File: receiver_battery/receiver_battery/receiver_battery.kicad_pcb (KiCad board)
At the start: 2 copper layers, 88 x 157 mm, 36 parts, among them U1 NRF24L01_Breakout

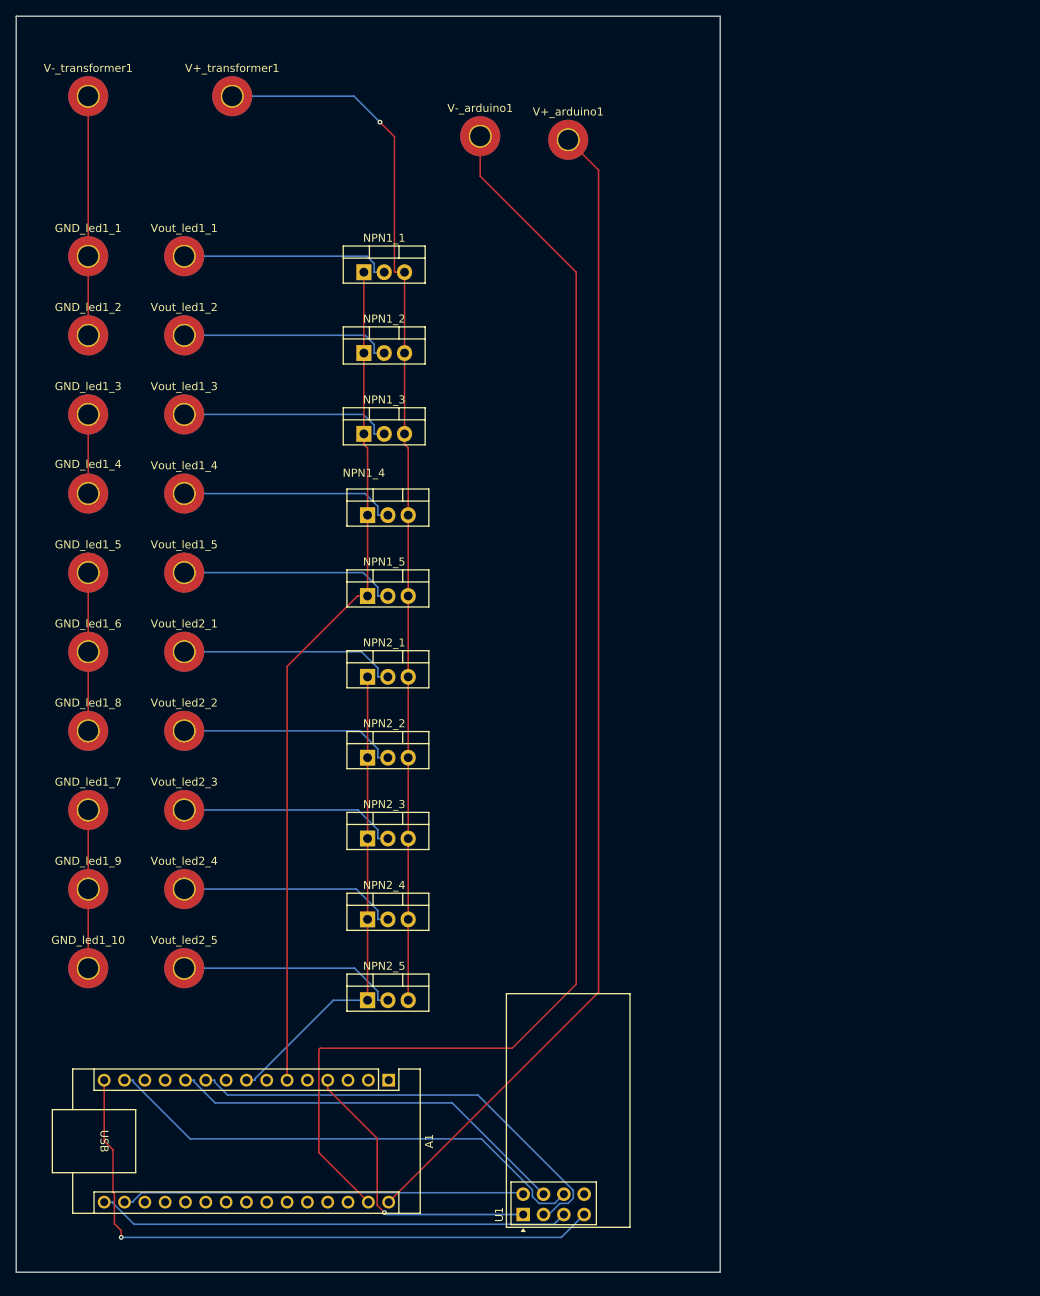
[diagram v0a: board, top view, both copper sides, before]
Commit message: pulldown on each transistor
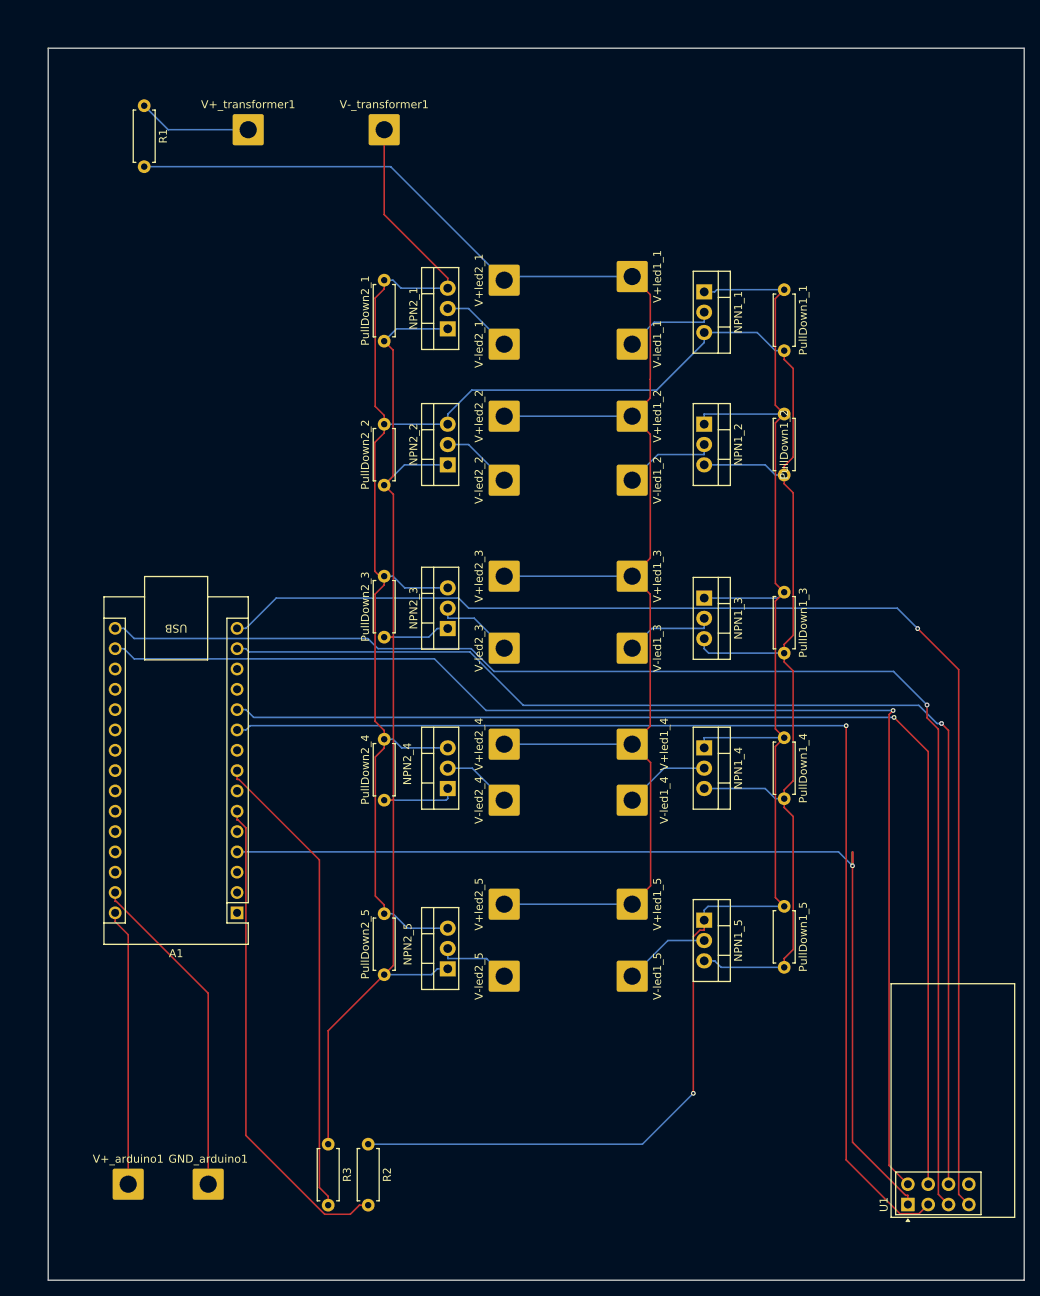
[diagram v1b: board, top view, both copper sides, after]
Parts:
- removed GND_led1_1, GND_led1_10, GND_led1_2, GND_led1_3, GND_led1_4, GND_led1_5, GND_led1_6, GND_led1_7, GND_led1_8, GND_led1_9, V-_arduino1, Vout_led1_1, Vout_led1_2, Vout_led1_3, Vout_led1_4, Vout_led1_5, Vout_led2_1, Vout_led2_2, Vout_led2_3, Vout_led2_4, Vout_led2_5: MountingHole_Pad, MountingHole:MountingHole_2.5mm_Pad_TopBottom
- added GND_arduino1: Conn_01x01_Pin, Connector_Wire:SolderWire-1.5sqmm_1x01_D1.7mm_OD3.9mm, F.Cu at (40.0, 183.0)
- added PullDown1_1: 10k, Resistor_THT:R_Axial_DIN0207_L6.3mm_D2.5mm_P7.62mm_Horizontal, F.Cu at (112.0, 71.2)
- added PullDown1_2: 10k, Resistor_THT:R_Axial_DIN0207_L6.3mm_D2.5mm_P7.62mm_Horizontal, F.Cu at (112.0, 86.7)
- added PullDown1_3: 10k, Resistor_THT:R_Axial_DIN0207_L6.3mm_D2.5mm_P7.62mm_Horizontal, F.Cu at (112.0, 109.0)
- added PullDown1_4: 10k, Resistor_THT:R_Axial_DIN0207_L6.3mm_D2.5mm_P7.62mm_Horizontal, F.Cu at (112.0, 127.2)
- added PullDown1_5: 10k, Resistor_THT:R_Axial_DIN0207_L6.3mm_D2.5mm_P7.62mm_Horizontal, F.Cu at (112.0, 148.3)
- added PullDown2_1: 10k, Resistor_THT:R_Axial_DIN0207_L6.3mm_D2.5mm_P7.62mm_Horizontal, F.Cu at (62.0, 77.6)
- added PullDown2_2: 10k, Resistor_THT:R_Axial_DIN0207_L6.3mm_D2.5mm_P7.62mm_Horizontal, F.Cu at (62.0, 95.6)
- added PullDown2_3: 10k, Resistor_THT:R_Axial_DIN0207_L6.3mm_D2.5mm_P7.62mm_Horizontal, F.Cu at (62.0, 114.6)
- added PullDown2_4: 10k, Resistor_THT:R_Axial_DIN0207_L6.3mm_D2.5mm_P7.62mm_Horizontal, F.Cu at (62.0, 135.0)
- added PullDown2_5: 10k, Resistor_THT:R_Axial_DIN0207_L6.3mm_D2.5mm_P7.62mm_Horizontal, F.Cu at (62.0, 156.8)
- added R1: R, Resistor_THT:R_Axial_DIN0207_L6.3mm_D2.5mm_P7.62mm_Horizontal, F.Cu at (32.0, 48.2)
- added R2: R, Resistor_THT:R_Axial_DIN0207_L6.3mm_D2.5mm_P7.62mm_Horizontal, F.Cu at (60.0, 178.0)
- added R3: R, Resistor_THT:R_Axial_DIN0207_L6.3mm_D2.5mm_P7.62mm_Horizontal, F.Cu at (55.0, 178.0)
- added V+led1_1: Conn_01x01_Pin, Connector_Wire:SolderWire-1.5sqmm_1x01_D1.7mm_OD3.9mm, F.Cu at (93.0, 69.5)
- added V+led1_2: Conn_01x01_Pin, Connector_Wire:SolderWire-1.5sqmm_1x01_D1.7mm_OD3.9mm, F.Cu at (93.0, 87.0)
- added V+led1_3: Conn_01x01_Pin, Connector_Wire:SolderWire-1.5sqmm_1x01_D1.7mm_OD3.9mm, F.Cu at (93.0, 107.0)
- added V+led1_4: Conn_01x01_Pin, Connector_Wire:SolderWire-1.5sqmm_1x01_D1.7mm_OD3.9mm, F.Cu at (93.0, 128.0)
- added V+led1_5: Conn_01x01_Pin, Connector_Wire:SolderWire-1.5sqmm_1x01_D1.7mm_OD3.9mm, F.Cu at (93.0, 148.0)
- added V+led2_1: Conn_01x01_Pin, Connector_Wire:SolderWire-1.5sqmm_1x01_D1.7mm_OD3.9mm, F.Cu at (77.0, 70.0)
- added V+led2_2: Conn_01x01_Pin, Connector_Wire:SolderWire-1.5sqmm_1x01_D1.7mm_OD3.9mm, F.Cu at (77.0, 87.0)
- added V+led2_3: Conn_01x01_Pin, Connector_Wire:SolderWire-1.5sqmm_1x01_D1.7mm_OD3.9mm, F.Cu at (77.0, 107.0)
- added V+led2_4: Conn_01x01_Pin, Connector_Wire:SolderWire-1.5sqmm_1x01_D1.7mm_OD3.9mm, F.Cu at (77.0, 128.0)
- added V+led2_5: Conn_01x01_Pin, Connector_Wire:SolderWire-1.5sqmm_1x01_D1.7mm_OD3.9mm, F.Cu at (77.0, 148.0)
- added V-led1_1: Conn_01x01_Pin, Connector_Wire:SolderWire-1.5sqmm_1x01_D1.7mm_OD3.9mm, F.Cu at (93.0, 78.0)
- added V-led1_2: Conn_01x01_Pin, Connector_Wire:SolderWire-1.5sqmm_1x01_D1.7mm_OD3.9mm, F.Cu at (93.0, 95.0)
- added V-led1_3: Conn_01x01_Pin, Connector_Wire:SolderWire-1.5sqmm_1x01_D1.7mm_OD3.9mm, F.Cu at (93.0, 116.0)
- added V-led1_4: Conn_01x01_Pin, Connector_Wire:SolderWire-1.5sqmm_1x01_D1.7mm_OD3.9mm, F.Cu at (93.0, 135.0)
- added V-led1_5: Conn_01x01_Pin, Connector_Wire:SolderWire-1.5sqmm_1x01_D1.7mm_OD3.9mm, F.Cu at (93.0, 157.0)
- added V-led2_1: Conn_01x01_Pin, Connector_Wire:SolderWire-1.5sqmm_1x01_D1.7mm_OD3.9mm, F.Cu at (77.0, 78.0)
- added V-led2_2: Conn_01x01_Pin, Connector_Wire:SolderWire-1.5sqmm_1x01_D1.7mm_OD3.9mm, F.Cu at (77.0, 95.0)
- added V-led2_3: Conn_01x01_Pin, Connector_Wire:SolderWire-1.5sqmm_1x01_D1.7mm_OD3.9mm, F.Cu at (77.0, 116.0)
- added V-led2_4: Conn_01x01_Pin, Connector_Wire:SolderWire-1.5sqmm_1x01_D1.7mm_OD3.9mm, F.Cu at (77.0, 135.0)
- added V-led2_5: Conn_01x01_Pin, Connector_Wire:SolderWire-1.5sqmm_1x01_D1.7mm_OD3.9mm, F.Cu at (77.0, 157.0)
- V+_arduino1, V+_transformer1, V-_transformer1: value MountingHole_Pad -> Conn_01x01_Pin; footprint MountingHole:MountingHole_2.5mm_Pad_TopBottom -> Connector_Wire:SolderWire-1.5sqmm_1x01_D1.7mm_OD3.9mm
- moved V+_arduino1 141.7 mm to (30.0, 183.0)
- moved NPN1_5 58.4 mm to (102.0, 150.0), turned to -90 degrees
- moved NPN1_4 51.2 mm to (102.0, 128.5), turned to -90 degrees
- moved U1 48.1 mm to (127.5, 185.5)
- moved NPN1_3 47.2 mm to (102.0, 109.7), turned to -90 degrees
- moved NPN2_1 44.6 mm to (69.9, 76.1), turned to 90 degrees
- moved NPN1_2 43.5 mm to (102.0, 88.0), turned to -90 degrees
- moved NPN1_1 42.6 mm to (102.0, 71.5), turned to -90 degrees
- moved NPN2_2 38.0 mm to (69.9, 93.1), turned to 90 degrees
- moved V-_transformer1 37.2 mm to (62.0, 51.2)
- moved A1 28.2 mm to (43.6, 149.1), turned to 180 degrees
- moved NPN2_3 28.1 mm to (69.9, 113.5), turned to 90 degrees
- moved NPN2_4 19.2 mm to (69.9, 133.5), turned to 90 degrees
- moved NPN2_5 10.8 mm to (69.9, 156.1), turned to 90 degrees
- moved V+_transformer1 4.64 mm to (45.0, 51.2)
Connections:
- A1 pad 6: pwm1 -> Net-(A1-D3)
- A1 pad 8: pwm2 -> Net-(A1-D5)
- NPN1_1 pad 3: VCC -> GND_transformer
- NPN1_2 pad 3: VCC -> GND_transformer
- NPN1_3 pad 3: VCC -> GND_transformer
- NPN1_4 pad 3: VCC -> GND_transformer
- NPN1_5 pad 3: VCC -> GND_transformer
- NPN2_1 pad 3: VCC -> GND_transformer
- NPN2_2 pad 3: VCC -> GND_transformer
- NPN2_3 pad 3: VCC -> GND_transformer
- NPN2_4 pad 3: VCC -> GND_transformer
- NPN2_5 pad 3: VCC -> GND_transformer
- V+_transformer1 pad 1: VCC -> Net-(V+_transformer1-Pin_1)
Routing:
- net GND_transformer: track 79.3 -> 321.4 mm
- net Net-(GND_arduino1-Pin_1): track 168.2 -> 41.4 mm
- net Net-(A1-VIN): track 145.2 -> 34.6 mm
- net Net-(A1-3V3): track 50.5 -> 160.8 mm, vias 0 -> 1
- net Net-(A1-D13): track 59.2 -> 169.0 mm, vias 0 -> 1
- net pwm1: track 106.1 -> 200.9 mm, vias 0 -> 1
- net Net-(U1-GND): track 36.9 -> 130.0 mm
- net Net-(A1-D8): track 50.8 -> 142.6 mm, vias 0 -> 1
- net pwm2: track 59.8 -> 151.0 mm
- net Net-(A1-D11): track 62.4 -> 149.9 mm, vias 0 -> 1
- net Net-(A1-D7): track 57.3 -> 144.2 mm, vias 0 -> 1
- net VCC: track 131.8 -> 217.0 mm, vias 1 -> 0
- net Net-(A1-D12): track 79.6 -> 162.9 mm
- net Net-(A1-D3): track 0.00 -> 60.9 mm
- net Net-(A1-D5): track 0.00 -> 59.2 mm
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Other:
- board size 88 x 157 mm -> 122 x 154 mm

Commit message: only 2 pull down res + res for each led
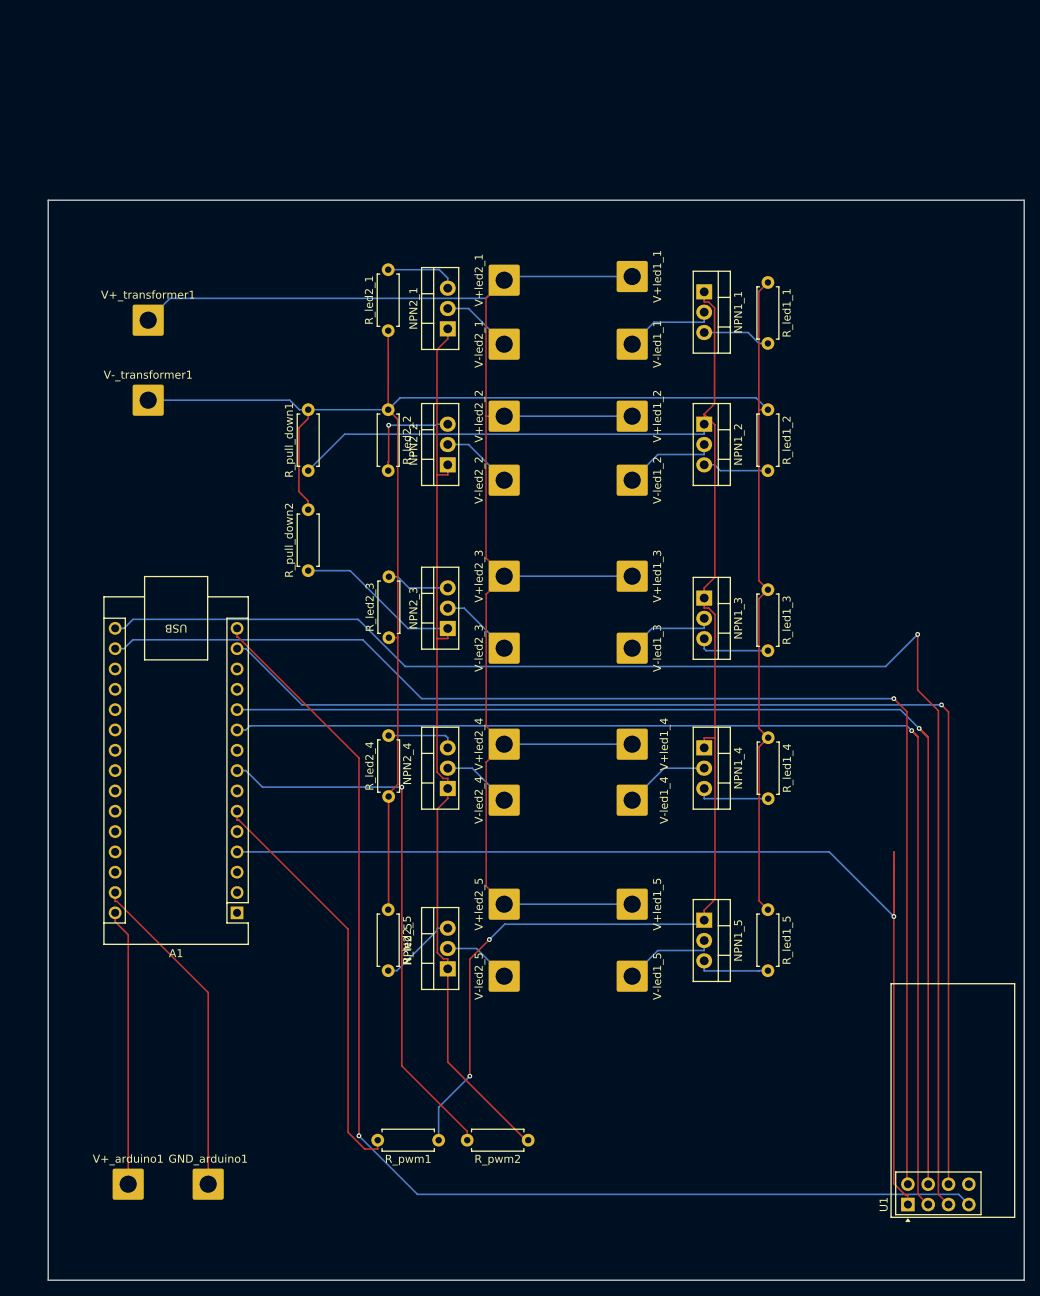
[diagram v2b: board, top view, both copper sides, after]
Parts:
- removed PullDown1_1, PullDown1_2, PullDown1_3, PullDown1_4, PullDown1_5, PullDown2_1, PullDown2_2, PullDown2_3, PullDown2_4, PullDown2_5: 10k, Resistor_THT:R_Axial_DIN0207_L6.3mm_D2.5mm_P7.62mm_Horizontal
- removed R1, R2, R3: R, Resistor_THT:R_Axial_DIN0207_L6.3mm_D2.5mm_P7.62mm_Horizontal
- added R_led1_1: 10k, Resistor_THT:R_Axial_DIN0207_L6.3mm_D2.5mm_P7.62mm_Horizontal, F.Cu at (110.0, 70.3)
- added R_led1_2: 10k, Resistor_THT:R_Axial_DIN0207_L6.3mm_D2.5mm_P7.62mm_Horizontal, F.Cu at (110.0, 86.2)
- added R_led1_3: 10k, Resistor_THT:R_Axial_DIN0207_L6.3mm_D2.5mm_P7.62mm_Horizontal, F.Cu at (110.0, 108.7)
- added R_led1_4: 10k, Resistor_THT:R_Axial_DIN0207_L6.3mm_D2.5mm_P7.62mm_Horizontal, F.Cu at (110.0, 127.2)
- added R_led1_5: 10k, Resistor_THT:R_Axial_DIN0207_L6.3mm_D2.5mm_P7.62mm_Horizontal, F.Cu at (110.0, 148.7)
- added R_led2_1: 10k, Resistor_THT:R_Axial_DIN0207_L6.3mm_D2.5mm_P7.62mm_Horizontal, F.Cu at (62.5, 76.3)
- added R_led2_2: 10k, Resistor_THT:R_Axial_DIN0207_L6.3mm_D2.5mm_P7.62mm_Horizontal, F.Cu at (62.5, 86.2)
- added R_led2_3: 10k, Resistor_THT:R_Axial_DIN0207_L6.3mm_D2.5mm_P7.62mm_Horizontal, F.Cu at (62.6, 114.7)
- added R_led2_4: 10k, Resistor_THT:R_Axial_DIN0207_L6.3mm_D2.5mm_P7.62mm_Horizontal, F.Cu at (62.6, 134.5)
- added R_led2_5: 10k, Resistor_THT:R_Axial_DIN0207_L6.3mm_D2.5mm_P7.62mm_Horizontal, F.Cu at (62.5, 148.7)
- added R_pull_down1: 10k, Resistor_THT:R_Axial_DIN0207_L6.3mm_D2.5mm_P7.62mm_Horizontal, F.Cu at (52.5, 93.8)
- added R_pull_down2: 10k, Resistor_THT:R_Axial_DIN0207_L6.3mm_D2.5mm_P7.62mm_Horizontal, F.Cu at (52.5, 106.3)
- added R_pwm1: R, Resistor_THT:R_Axial_DIN0207_L6.3mm_D2.5mm_P7.62mm_Horizontal, F.Cu at (68.8, 177.5)
- added R_pwm2: R, Resistor_THT:R_Axial_DIN0207_L6.3mm_D2.5mm_P7.62mm_Horizontal, F.Cu at (80.0, 177.5)
- moved V-_transformer1 44.9 mm to (32.5, 85.0)
- moved V+_transformer1 26.9 mm to (32.5, 75.0)
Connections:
- net pwm1 renamed pd_1_in
- net pwm2 renamed pd_2_in
- NPN1_1 pad 3: GND_transformer -> Net-(NPN1_1-S)
- NPN1_2 pad 3: GND_transformer -> Net-(NPN1_2-S)
- NPN1_3 pad 3: GND_transformer -> Net-(NPN1_3-S)
- NPN1_4 pad 3: GND_transformer -> Net-(NPN1_4-S)
- NPN1_5 pad 3: GND_transformer -> Net-(NPN1_5-S)
- NPN2_1 pad 3: GND_transformer -> Net-(NPN2_1-S)
- NPN2_2 pad 3: GND_transformer -> Net-(NPN2_2-S)
- NPN2_3 pad 3: GND_transformer -> Net-(NPN2_3-S)
- NPN2_4 pad 3: GND_transformer -> Net-(NPN2_4-S)
- NPN2_5 pad 3: GND_transformer -> Net-(NPN2_5-S)
- V+_transformer1 pad 1: Net-(V+_transformer1-Pin_1) -> VCC
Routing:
- net GND_transformer: track 321.4 -> 249.5 mm
- net Net-(U1-GND): track 130.0 -> 154.7 mm
- net pd_2_in: track 151.0 -> 134.2 mm
- net Net-(V+_transformer1-Pin_1): track 14.2 -> 0.00 mm
- net Net-(A1-D12): track 162.9 -> 149.6 mm
- net Net-(NPN2_2-S): track 0.00 -> 13.1 mm, vias 0 -> 1
- net Net-(NPN2_5-S): track 0.00 -> 9.80 mm
- net Net-(A1-D5): track 59.2 -> 69.0 mm, vias 0 -> 1
- net Net-(NPN1_3-S): track 0.00 -> 9.32 mm
- net Net-(NPN1_4-S): track 0.00 -> 9.26 mm
- net Net-(NPN1_5-S): track 0.00 -> 9.23 mm
- net Net-(A1-D3): track 60.9 -> 51.7 mm
- net Net-(NPN2_1-S): track 0.00 -> 9.14 mm
- net Net-(NPN2_4-S): track 0.00 -> 8.76 mm
- net Net-(A1-D13): track 169.0 -> 177.8 mm
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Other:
- board size 122 x 154 mm -> 122 x 135 mm

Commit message: large cock resistor
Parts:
- R_led1_1, R_led1_2, R_led1_3, R_led1_4, R_led1_5, R_led2_1, R_led2_2, R_led2_3, R_led2_4, R_led2_5: footprint Resistor_THT:R_Axial_DIN0207_L6.3mm_D2.5mm_P7.62mm_Horizontal -> Resistor_THT:R_Axial_Power_L20.0mm_W6.4mm_P7.62mm_Vertical
- moved R_led2_5 1.83 mm to (62.2, 150.5)
- moved R_led2_2 1.47 mm to (62.2, 87.6)
- moved R_led1_2 1.44 mm to (110.0, 87.6)
- moved R_led2_1 1.19 mm to (62.2, 77.5)
- moved R_led1_5 0.90 mm to (110.0, 149.6)
- moved R_led1_4 0.47 mm to (109.9, 127.6)
- moved R_led2_4 0.35 mm to (62.6, 134.9)
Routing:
- net Net-(U1-GND): track 154.7 -> 115.7 mm
- net Net-(A1-D11): track 151.2 -> 180.3 mm
- net Net-(A1-D7): track 149.4 -> 127.7 mm
- net Net-(A1-D8): track 150.1 -> 171.6 mm
- net Net-(A1-D12): track 149.6 -> 163.1 mm
- net Net-(A1-D5): track 69.0 -> 58.1 mm, vias 1 -> 0
- net Net-(GND_arduino1-Pin_1): track 41.4 -> 47.8 mm
- net VCC: track 212.6 -> 218.0 mm
- net pd_1_in: track 194.8 -> 189.6 mm, vias 2 -> 0
- net Net-(A1-D13): track 177.8 -> 172.7 mm
- net Net-(A1-D3): track 51.7 -> 48.4 mm
- net GND_transformer: track 249.5 -> 252.5 mm
- net Net-(NPN2_5-S): track 9.80 -> 11.6 mm
- net Net-(NPN1_2-S): track 8.27 -> 10.0 mm
- net Net-(NPN2_2-S): track 13.1 -> 11.7 mm, vias 1 -> 0
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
